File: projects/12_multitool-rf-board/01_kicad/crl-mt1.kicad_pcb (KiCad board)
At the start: 4 copper layers, 110 x 66 mm, 87 parts, among them M1 vibro, SW1 RFswitch, SW2 RFswitch, U1 STM32WB55RG, U10 ESD, U2 CC1101, U3 ST25R3916, U5 ST7565R, U6 BQ25896, U7 BQ27220, U8 LM3281, U8B LM3281, U9 loadsw, X10 BAT+NTC, X6 FFC 18p, Y1 32MHz, Y2 32.768kHz

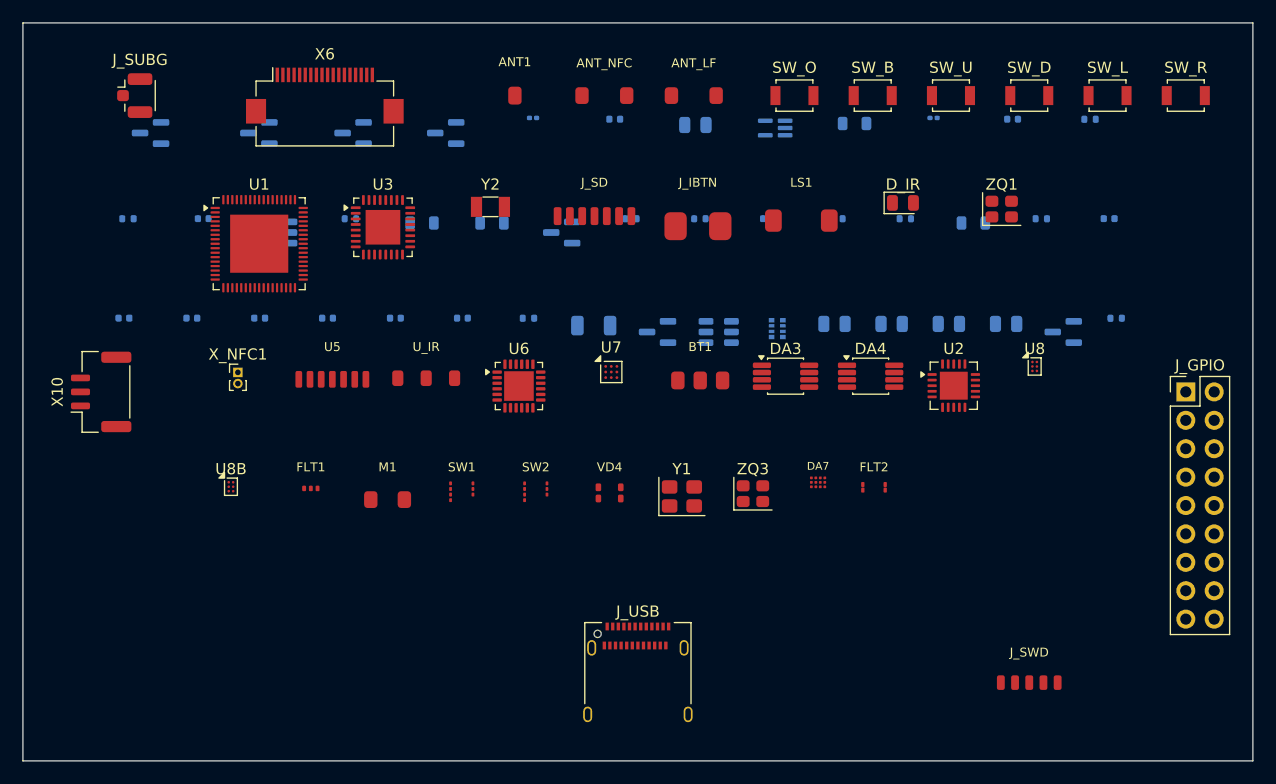
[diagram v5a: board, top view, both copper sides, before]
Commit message: proj12: smaller board 100x60mm, crystals clustered under their ICs
- crystal-cluster packing: Y1/Y2 under U1, ZQ3 under U2, ZQ1 under U3 (short
  OSC nets, signal integrity; fixes the LSE_OUT routing block)
- battery pack BT1 now off-board (external, wired via X10) - frees board area
- op-amps/DFN moved to bottom side, tighter GAP 0.7, INSET 5
- board 100x60mm (was 110x66) ~17% smaller; check_assembly: buildable
  (0 overlap, 0 off-board), 86 populated parts

Co-Authored-By: Claude Opus 4.8 <noreply@anthropic.com>
Claude-Session: https://claude.ai/code/session_01Hk6s8R6up8HYVQWXd3atVk
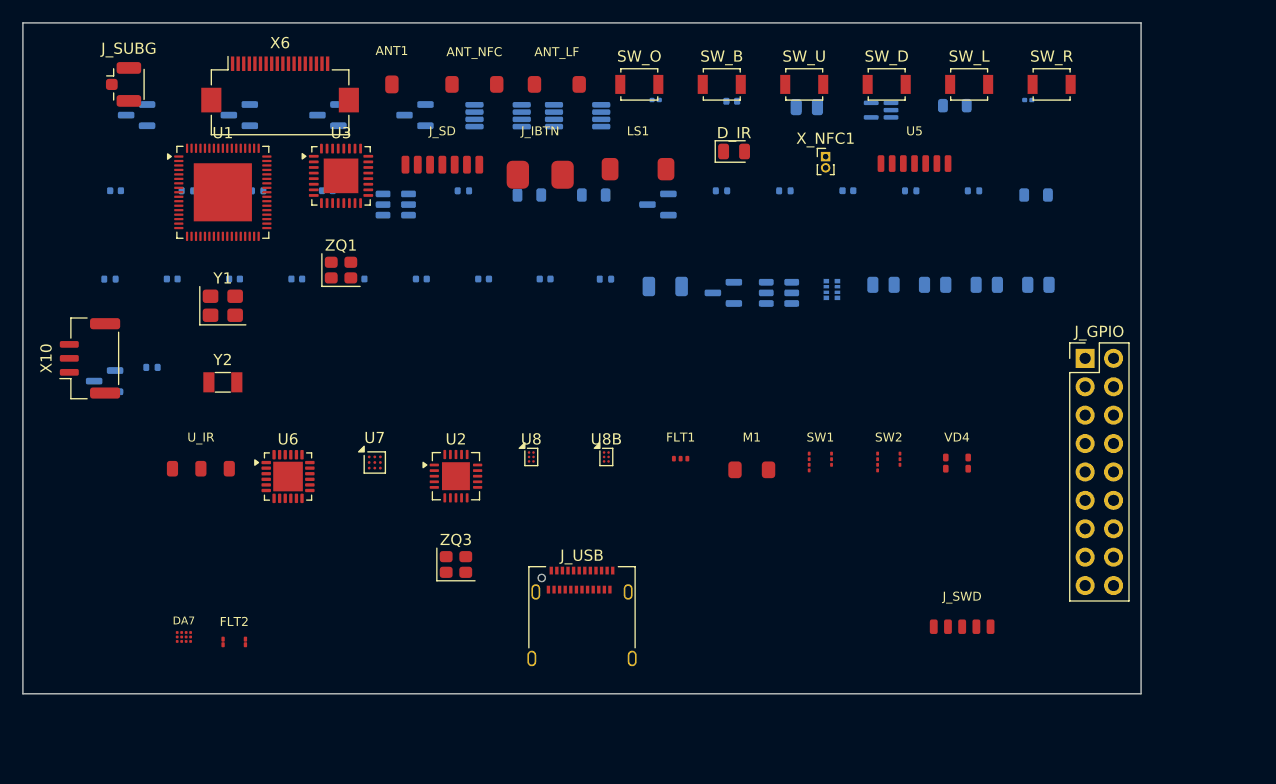
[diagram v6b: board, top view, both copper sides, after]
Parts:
- removed BT1: Li-Po 1S, crl-mt1:Battery_3p
- DA3, DA4: moved to B.Cu
- moved R13 86.3 mm to (41.5, 60.8)
- moved Q_IR 85.8 mm to (37.3, 62.0)
- moved C1 84.0 mm to (43.4, 52.9)
- moved R_FGB 83.5 mm to (37.8, 52.9)
- moved R_MID1 81.0 mm to (44.7, 45.0)
- moved C_AGDC 80.5 mm to (38.3, 45.0)
- moved ZQ1 59.3 mm to (58.4, 52.1)
- moved FLT2 58.9 mm to (48.9, 85.4)
- moved DA7 58.4 mm to (44.4, 84.9)
- moved X_NFC1 56.0 mm to (101.8, 42.0)
- moved U5 55.5 mm to (109.7, 42.6)
- moved U8 45.7 mm to (75.5, 68.8)
- moved U2 45.2 mm to (68.7, 70.5)
- moved Y1 44.5 mm to (47.9, 55.3)
- moved DA4 35.1 mm to (79.6, 38.3), turned to 180 degrees
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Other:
- board size 110 x 66 mm -> 100 x 60 mm
